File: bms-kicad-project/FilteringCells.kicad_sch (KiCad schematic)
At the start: 48 parts, among them J1 S7B-XH-A, Q1 BSS308PE_H6327, Q2 BSS308PE_H6327, Q3 BSS308PE_H6327, Q5 BSS308PE_H6327, Q6 BSS308PE_H6327, Q7 BSS308PE_H6327

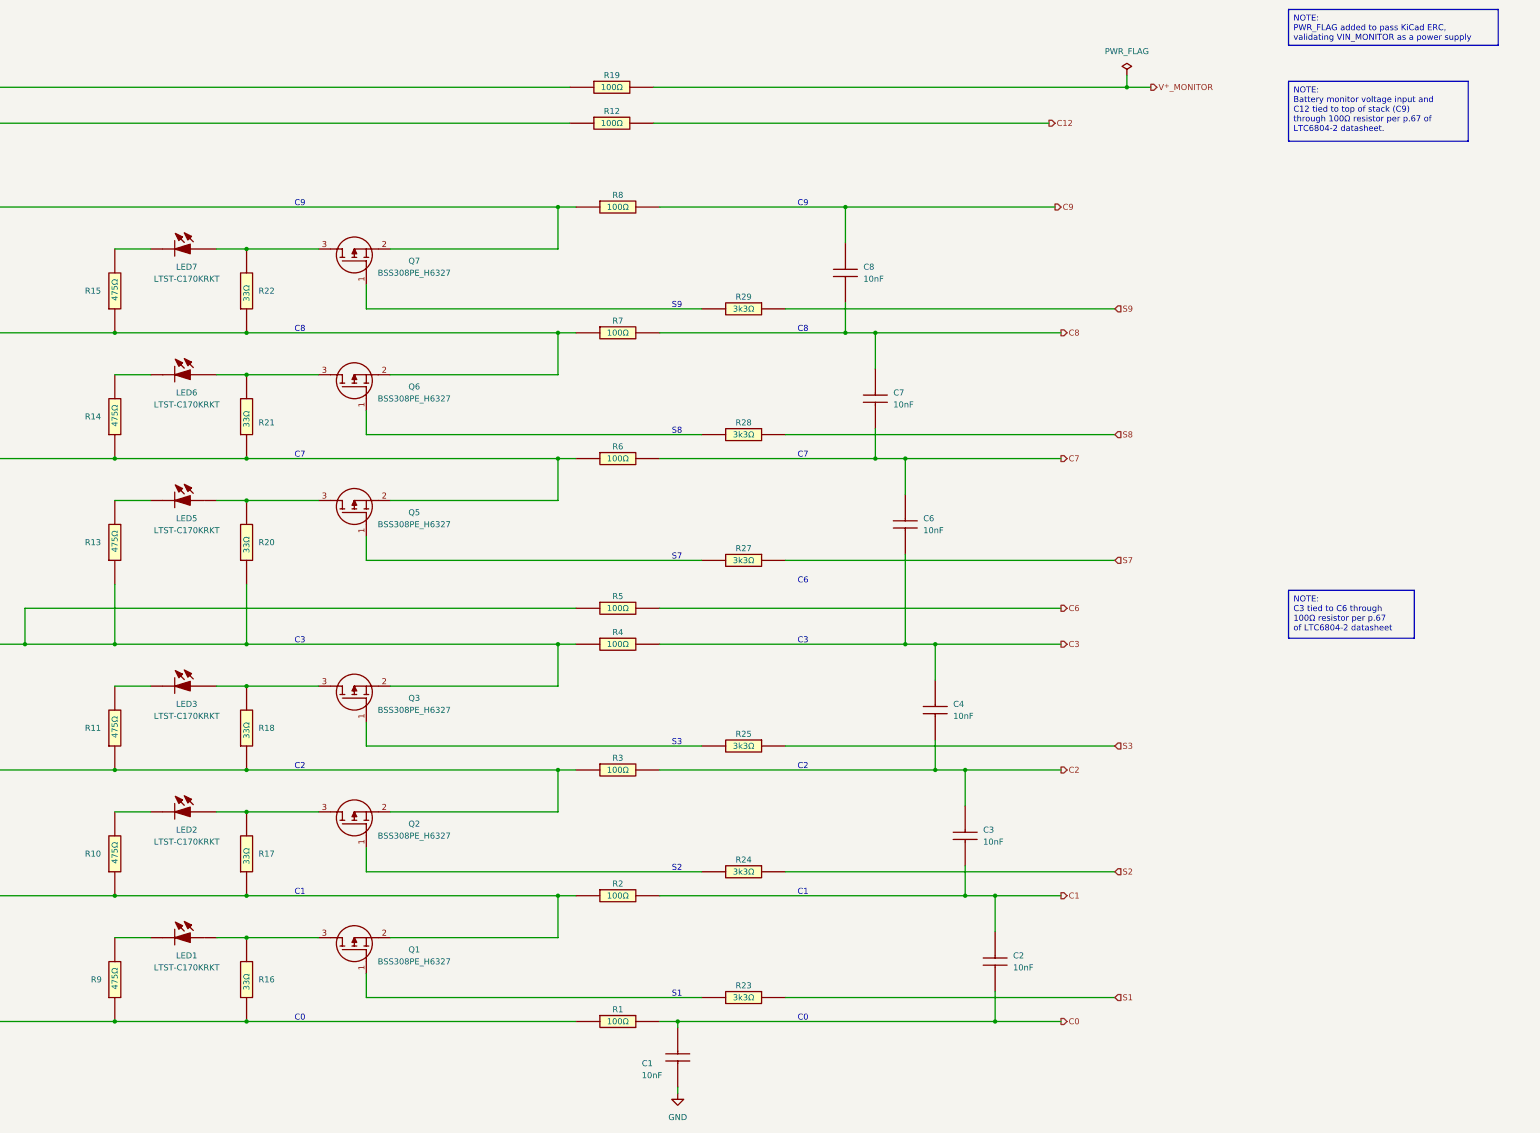
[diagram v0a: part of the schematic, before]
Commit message: feat: added minimal MCU schematic, 3D component model folder
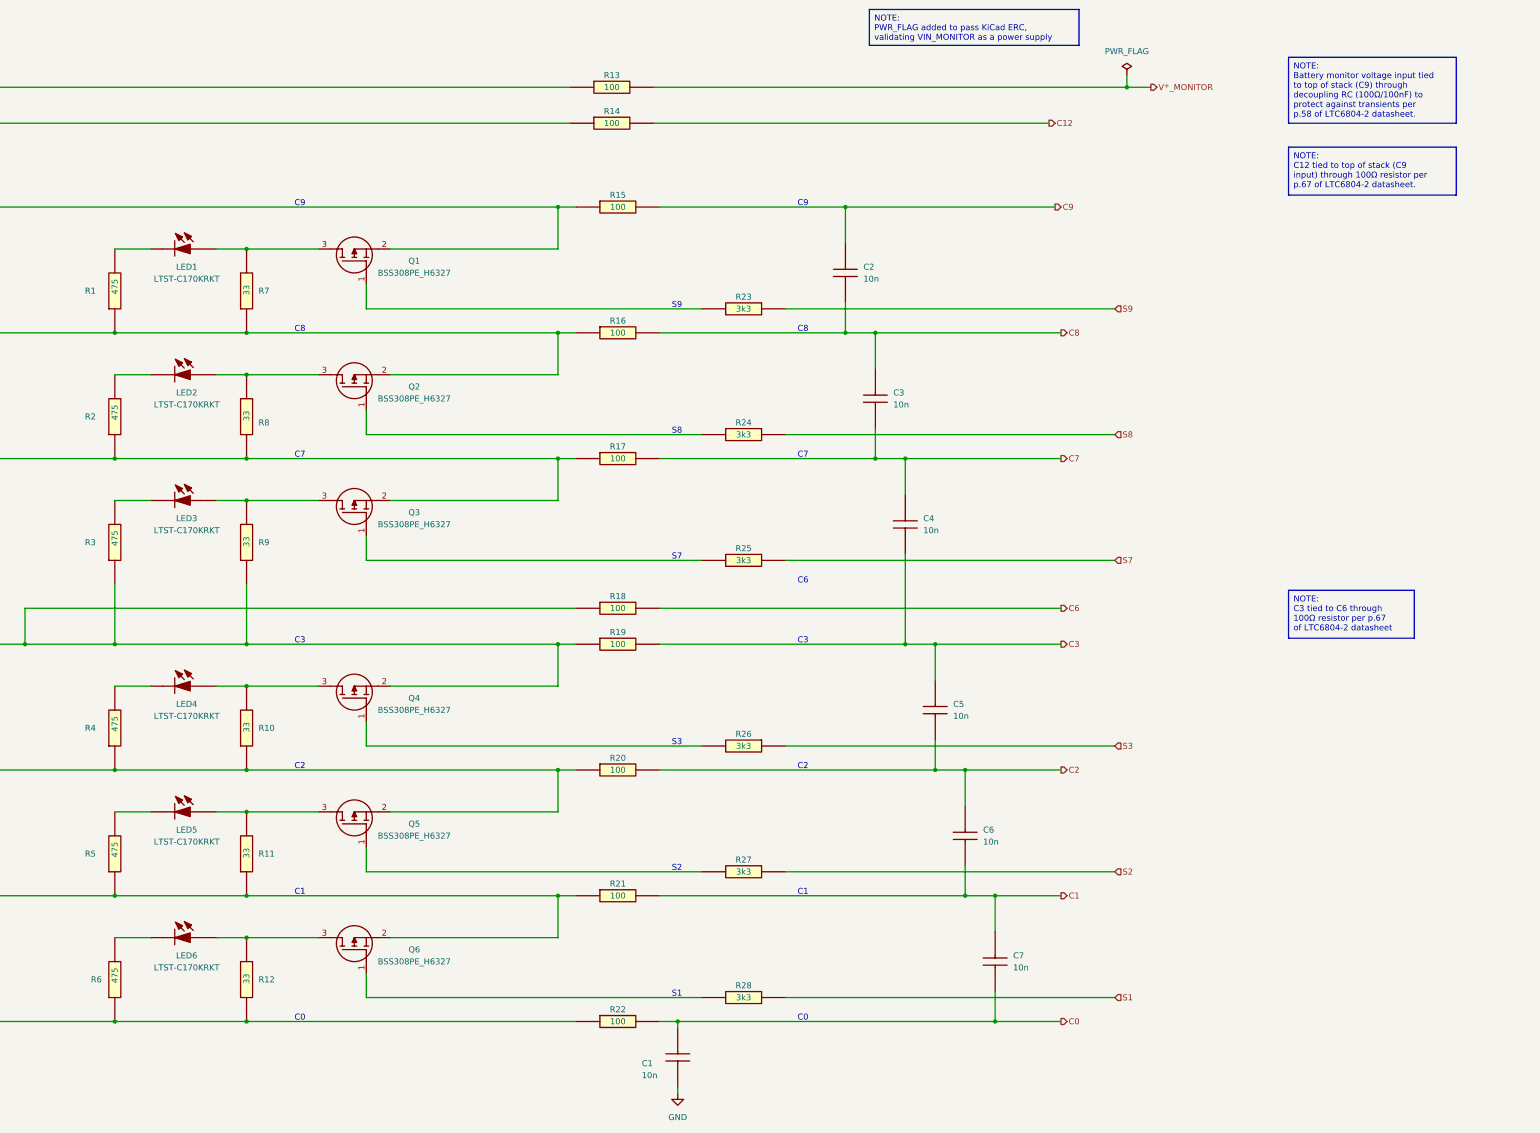
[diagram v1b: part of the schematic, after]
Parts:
- C1: value 10nF -> 10n
- C2: renamed from C8; value 10nF -> 10n
- C3: renamed from C7; value 10nF -> 10n
- C4: renamed from C6; value 10nF -> 10n
- C5: renamed from C4; value 10nF -> 10n
- C6: renamed from C3; value 10nF -> 10n
- C7: renamed from C2; value 10nF -> 10n
- R1: renamed from R15; value 475Ω -> 475
- R10: renamed from R18; value 33Ω -> 33; footprint RESC6332X70N -> FixedWing:RESC6332X70N
- R11: renamed from R17; value 33Ω -> 33; footprint RESC6332X70N -> FixedWing:RESC6332X70N
- R12: renamed from R16; value 33Ω -> 33; footprint RESC6332X70N -> FixedWing:RESC6332X70N
- R13: renamed from R19; value 100Ω -> 100
- R14: renamed from R12; value 100Ω -> 100
- R15: renamed from R8; value 100Ω -> 100
- R16: renamed from R7; value 100Ω -> 100
- R17: renamed from R6; value 100Ω -> 100
- R18: renamed from R5; value 100Ω -> 100
- R19: renamed from R4; value 100Ω -> 100
- R2: renamed from R14; value 475Ω -> 475
- R20: renamed from R3; value 100Ω -> 100
- R21: renamed from R2; value 100Ω -> 100
- R22: renamed from R1; value 100Ω -> 100
- R23: renamed from R29; value 3k3Ω -> 3k3
- R24: renamed from R28; value 3k3Ω -> 3k3
- R25: renamed from R27; value 3k3Ω -> 3k3
- R26: renamed from R25; value 3k3Ω -> 3k3
- R27: renamed from R24; value 3k3Ω -> 3k3
- R28: renamed from R23; value 3k3Ω -> 3k3
- R3: renamed from R13; value 475Ω -> 475
- R4: renamed from R11; value 475Ω -> 475
- R5: renamed from R10; value 475Ω -> 475
- R6: renamed from R9; value 475Ω -> 475
- R7: renamed from R22; value 33Ω -> 33; footprint RESC6332X70N -> FixedWing:RESC6332X70N
- R8: renamed from R21; value 33Ω -> 33; footprint RESC6332X70N -> FixedWing:RESC6332X70N
- R9: renamed from R20; value 33Ω -> 33; footprint RESC6332X70N -> FixedWing:RESC6332X70N
- renumbered LED7 to LED1, LED6 to LED2, LED5 to LED3, LED3 to LED4, LED2 to LED5, LED1 to LED6, Q7 to Q1, Q6 to Q2, Q5 to Q3, Q3 to Q4, Q2 to Q5, Q1 to Q6

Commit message: feat:continuing work on integrating RP2040 MCU
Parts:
- added C29: 0.1µ, FixedWing:G-21_MUR, symbol FixedWing:GCM21BR72A104KA37L
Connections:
- net GND: now also C29.1
- net V^{+}_MONITOR: now also C29.2
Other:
- moved on the sheet: R13, R14

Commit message: feat: Added 3D models for connector and Flash ROM
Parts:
- J1: Manufacture_Part_Number (none) -> S7B-XH-A; Manufacturer (none) -> JST Sales America Inc.; Manufacturer Part Number (none) -> S7B-XH-A
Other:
- moved on the sheet: J1
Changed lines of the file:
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@@
     )
   )
-  (symbol (lib_id "FixedWing:S7B-XH-A") (at 41.91 160.02 180) (unit 1)
+  (symbol (lib_id "FixedWing:S7B-XH-A") (at 26.67 165.1 0) (unit 1)
     (in_bom yes) (on_board yes) (dnp no) (fields_autoplaced)
     (property "Reference" "J1" (at 33.02 137.16 0)
@@
       (effects (font (size 1.524 1.524)))
     )
-    (property "Footprint" "CONN_S7B-XH-A_JST" (at 45.72 166.37 0)
+    (property "Footprint" "CONN_S7B-XH-A_JST" (at 22.86 158.75 0)
       (effects (font (size 1.27 1.27) italic) hide)
     )
-    (property "Datasheet" "S7B-XH-A" (at 45.72 163.83 0)
+    (property "Datasheet" "S7B-XH-A" (at 22.86 161.29 0)
       (effects (font (size 1.27 1.27) italic) hide)
     )
+    (property "Manufacturer" "JST Sales America Inc." (at 26.67 165.1 0)
+      (effects (font (size 1.27 1.27)) hide)
+    )
+    (property "Manufacturer Part Number" "S7B-XH-A" (at 26.67 165.1 0)
+      (effects (font (size 1.27 1.27)) hide)
+    )
+    (property "Manufacture_Part_Number" "S7B-XH-A" (at 13.97 156.21 0)
+      (effects (font (size 1.27 1.27)) hide)
+    )
     (pin "5")

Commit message: feat: finished preliminary RP2040 schematic design
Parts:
- removed C29: 0.1µ, FixedWing:G-21_MUR, symbol FixedWing:GCM21BR72A104KA37L
- removed R13: 100, RESC2012X50N, symbol FixedWing:CRCW0805100RFKEA
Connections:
- net +BATT: now reaches J1.7, Q1.2 (S), R14.1, R15.1
